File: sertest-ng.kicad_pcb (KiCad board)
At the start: 4 copper layers, 50 x 160 mm, 145 parts, among them J101 SWD, J102 USB, J201 Debug, J202 RS-232, J203 RS-485/422, J301 USB, J401 CAN, J402 CAN, SW101 Reset, SW401 Term, U101 M24C64-RMN, U102 AMS1117-3.3, U103 STM32G431RBTx, U104 ATECC608B-MAVDA-S, U105 USBLC6-2SC6, U201 ADM213, U202 SP330, U301 XC6206P332MR, U302 CH340N, U303 USBLC6-2SC6, U401 TJA1042T, Y101 8MHz, Y102 32k

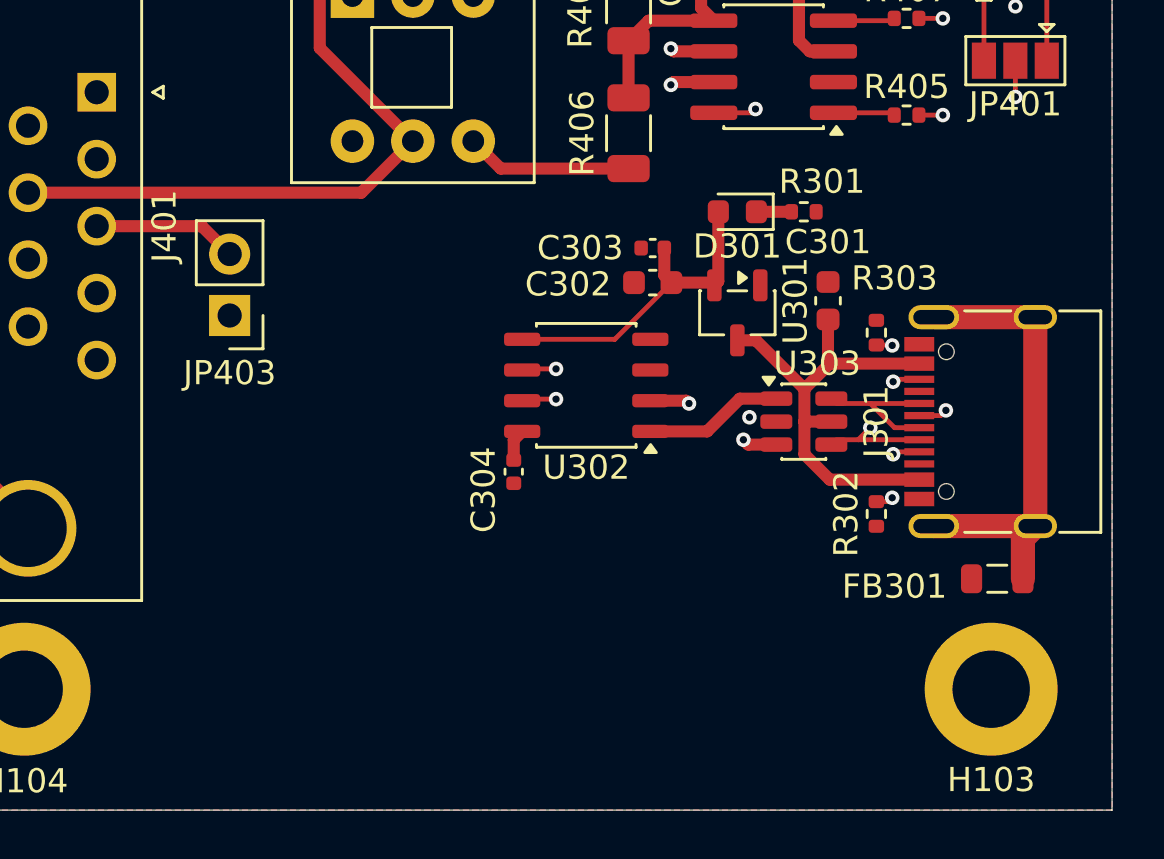
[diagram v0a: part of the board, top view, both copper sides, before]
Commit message: Revisit 3D models
Signed-off-by: Benedikt Spranger <b.spranger@linutronix.de>
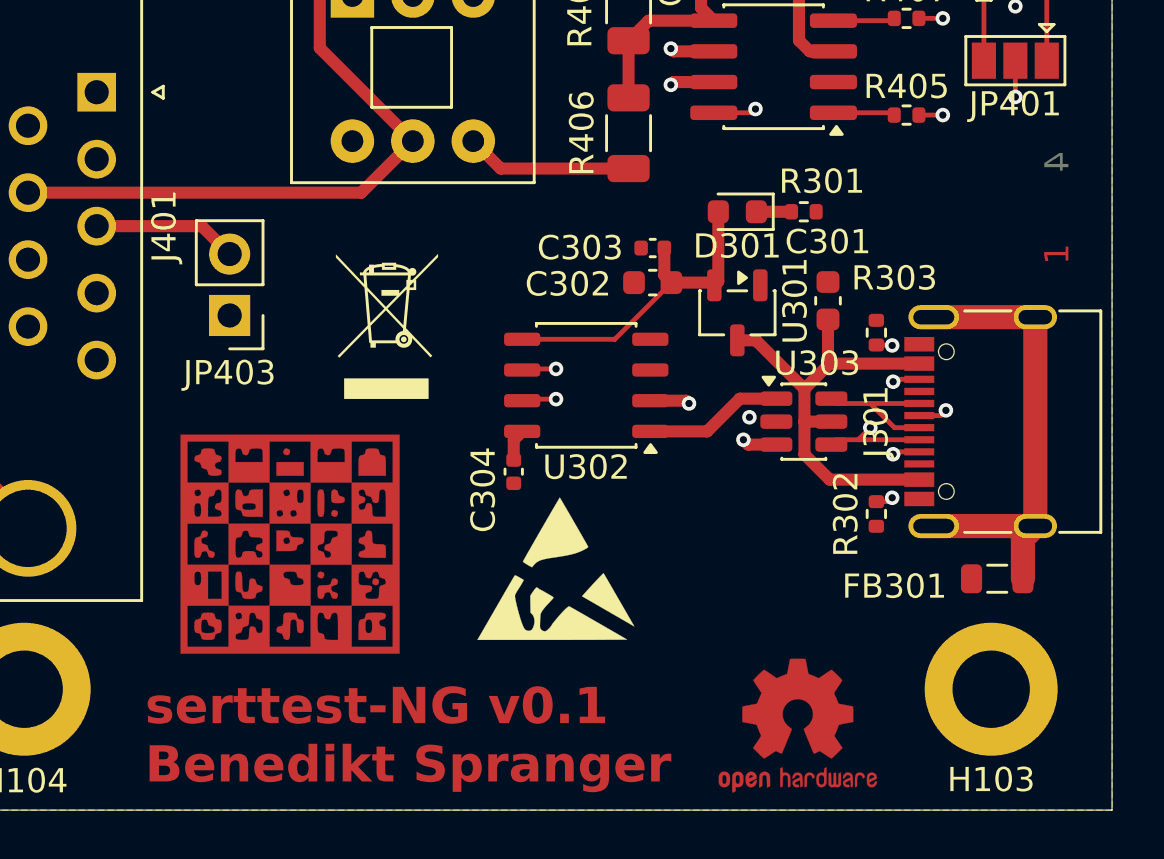
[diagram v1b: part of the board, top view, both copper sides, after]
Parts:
- added G***: LOGO, eurovibes:LOGO, F.Cu at (106.0, 169.0)
- added REF**: OSHW-Logo2_7.3x6mm_Copper, Symbol:OSHW-Logo2_7.3x6mm_Copper, F.Cu at (127.0, 176.5)
- added REF**: LayerMarker_4_6.35x2.54mm_TextH1mm_P1.27mm_BottomMirrored, Symbol:LayerMarker_4_6.35x2.54mm_TextH1mm_P1.27mm_BottomMirrored, F.Cu at (139.0, 157.0)
- added REF**: WEEE-Logo_4.2x6mm_SilkScreen, Symbol:WEEE-Logo_4.2x6mm_SilkScreen, F.Cu at (110.0, 160.0)
- added REF**: ESD-Logo_6.6x6mm_SilkScreen, Symbol:ESD-Logo_6.6x6mm_SilkScreen, F.Cu at (117.0, 170.0)
- D201, D202, D203, D204, D205, D206, D207, D208, D209, D210, D211, D212, D213, D214, D401, D402: footprint LED_SMD:LED_Kingbright_AAA3528ESGCT -> fixes:LED_Kingbright_AAA3528ESGCT
- J203: footprint TerminalBlock_WAGO:TerminalBlock_WAGO_236-404_1x04_P5.00mm_45Degree -> fixes:TerminalBlock_WAGO_236-404_1x04_P5.00mm_45Degree
- J402: footprint TerminalBlock_WAGO:TerminalBlock_WAGO_236-402_1x02_P5.00mm_45Degree -> fixes:TerminalBlock_WAGO_236-402_1x02_P5.00mm_45Degree
- SW401: footprint Button_Switch_THT:SW_Push_2P2T_Toggle_CK_PVA2xxH1xxxxxxV2 -> fixes:SW_Push_2P2T_Toggle_CK_PVA2xxH1xxxxxxV2
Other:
- board text added: "serttest-NG v0.1 Benedikt Spranger"

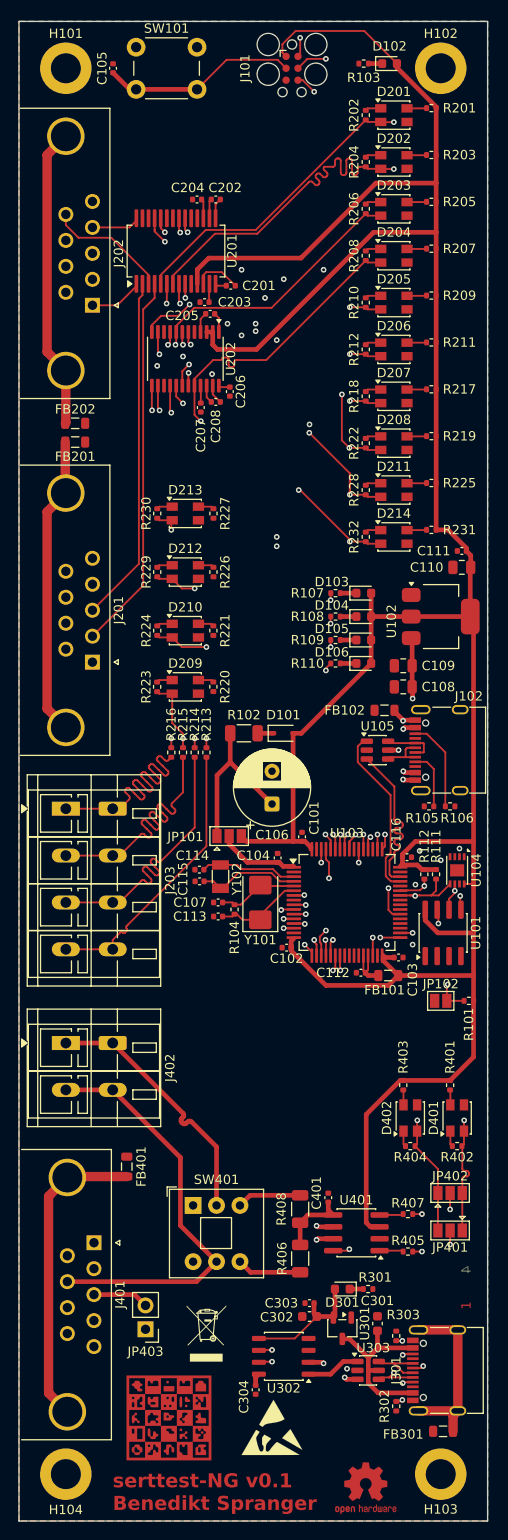
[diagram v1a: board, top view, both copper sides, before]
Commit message: Fix Dual LED footprint issue
Signed-off-by: Benedikt Spranger <b.spranger@linutronix.de>
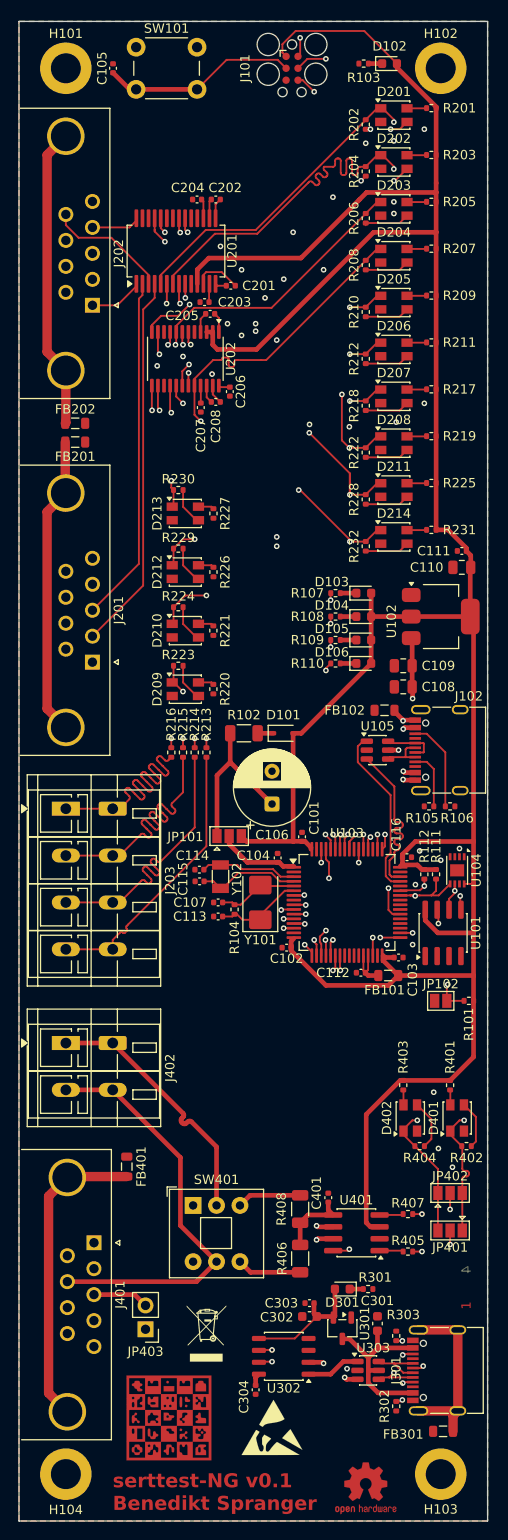
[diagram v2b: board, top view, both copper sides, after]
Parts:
- moved R224 3.36 mm to (107.0, 82.5), turned to 0 degrees
- moved R229 3.36 mm to (107.0, 76.2), turned to 0 degrees
- moved R230 3.36 mm to (107.0, 70.0), turned to 0 degrees
- moved R223 3.19 mm to (107.0, 88.8), turned to 0 degrees
- moved R202 1.00 mm to (127.0, 31.0), turned to -90 degrees
- moved R204 1.00 mm to (127.0, 36.0), turned to -90 degrees
- moved R206 1.00 mm to (127.0, 41.0), turned to -90 degrees
- moved R208 1.00 mm to (127.0, 46.0), turned to -90 degrees
- moved R210 1.00 mm to (127.0, 51.0), turned to -90 degrees
- moved R212 1.00 mm to (127.0, 56.0), turned to -90 degrees
- moved R218 1.00 mm to (127.0, 61.0), turned to -90 degrees
- moved R222 1.00 mm to (127.0, 66.0), turned to -90 degrees
- moved R228 1.00 mm to (127.0, 71.0), turned to -90 degrees
- moved R232 1.00 mm to (127.0, 76.0), turned to -90 degrees
- moved R402 1.00 mm to (137.8, 140.0), turned to 0 degrees
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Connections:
- D201 pad 1: Net-(D201-A1) -> /USART3_RX
- D201 pad 3: GND -> Net-(D201-A1)
- D201 pad 4: /USART3_RX -> GND
- D202 pad 1: Net-(D202-A1) -> /USART3_TX
- D202 pad 3: GND -> Net-(D202-A1)
- D202 pad 4: /USART3_TX -> GND
- D203 pad 1: Net-(D203-A1) -> /USART2_RX
- D203 pad 3: GND -> Net-(D203-A1)
- D203 pad 4: /USART2_RX -> GND
- D204 pad 1: Net-(D204-A1) -> /USART2_TX
- D204 pad 3: GND -> Net-(D204-A1)
- D204 pad 4: /USART2_TX -> GND
- D205 pad 1: Net-(D205-A1) -> /USART2_CTS
- D205 pad 3: GND -> Net-(D205-A1)
- D205 pad 4: /USART2_CTS -> GND
- D206 pad 1: Net-(D206-A1) -> /USART2_RTS
- D206 pad 3: GND -> Net-(D206-A1)
- D206 pad 4: /USART2_RTS -> GND
- D207 pad 1: Net-(D207-A1) -> /USART2_DCD
- D207 pad 3: GND -> Net-(D207-A1)
- D207 pad 4: /USART2_DCD -> GND
- D208 pad 1: Net-(D208-A1) -> /USART2_DSR
- D208 pad 3: GND -> Net-(D208-A1)
- D208 pad 4: /USART2_DSR -> GND
- D209 pad 1: Net-(D209-A1) -> /Serial/TXD
- D209 pad 3: GND -> Net-(D209-A1)
- D209 pad 4: /Serial/TXD -> GND
- D210 pad 1: Net-(D210-A1) -> /Serial/RXD
- D210 pad 3: GND -> Net-(D210-A1)
- D210 pad 4: /Serial/RXD -> GND
- D211 pad 1: Net-(D211-A1) -> /USART2_DTR
- D211 pad 3: GND -> Net-(D211-A1)
- D211 pad 4: /USART2_DTR -> GND
- D212 pad 1: Net-(D212-A1) -> /Serial/CTS
- D212 pad 3: GND -> Net-(D212-A1)
- D212 pad 4: /Serial/CTS -> GND
- D213 pad 1: Net-(D213-A1) -> /Serial/RTS
- D213 pad 3: GND -> Net-(D213-A1)
- D213 pad 4: /Serial/RTS -> GND
- D214 pad 1: Net-(D214-A1) -> /USART2_RI
- D214 pad 3: GND -> Net-(D214-A1)
- D214 pad 4: /USART2_RI -> GND
- D401 pad 1: Net-(D401-A1) -> /FDCAN1_TX
- D401 pad 3: GND -> Net-(D401-A1)
- D401 pad 4: /FDCAN1_TX -> GND
- D402 pad 1: Net-(D402-A1) -> /FDCAN1_RX
- D402 pad 3: GND -> Net-(D402-A1)
- D402 pad 4: /FDCAN1_RX -> GND
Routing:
- net Net-(D202-A1): track 1.69 -> 6.13 mm, vias 0 -> 2
- net Net-(D402-A1): track 1.69 -> 5.34 mm
- net /Serial/TXD: track 69.2 -> 65.7 mm, vias 2 -> 3
- net Net-(D203-A1): track 1.69 -> 5.18 mm
- net Net-(D401-A1): track 1.69 -> 5.13 mm
- net Net-(D214-A1): track 1.69 -> 4.73 mm
- net Net-(D211-A1): track 1.69 -> 4.73 mm
- net Net-(D208-A1): track 1.69 -> 4.73 mm
- net Net-(D201-A1): track 1.69 -> 4.73 mm, vias 0 -> 2
- net Net-(D207-A1): track 1.69 -> 4.73 mm
- net Net-(D206-A1): track 1.69 -> 4.73 mm
- net Net-(D205-A1): track 1.69 -> 4.73 mm
- net Net-(D204-A1): track 1.69 -> 4.73 mm
- net Net-(D213-A1): track 1.69 -> 4.02 mm
- net Net-(D212-A1): track 1.69 -> 4.02 mm
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
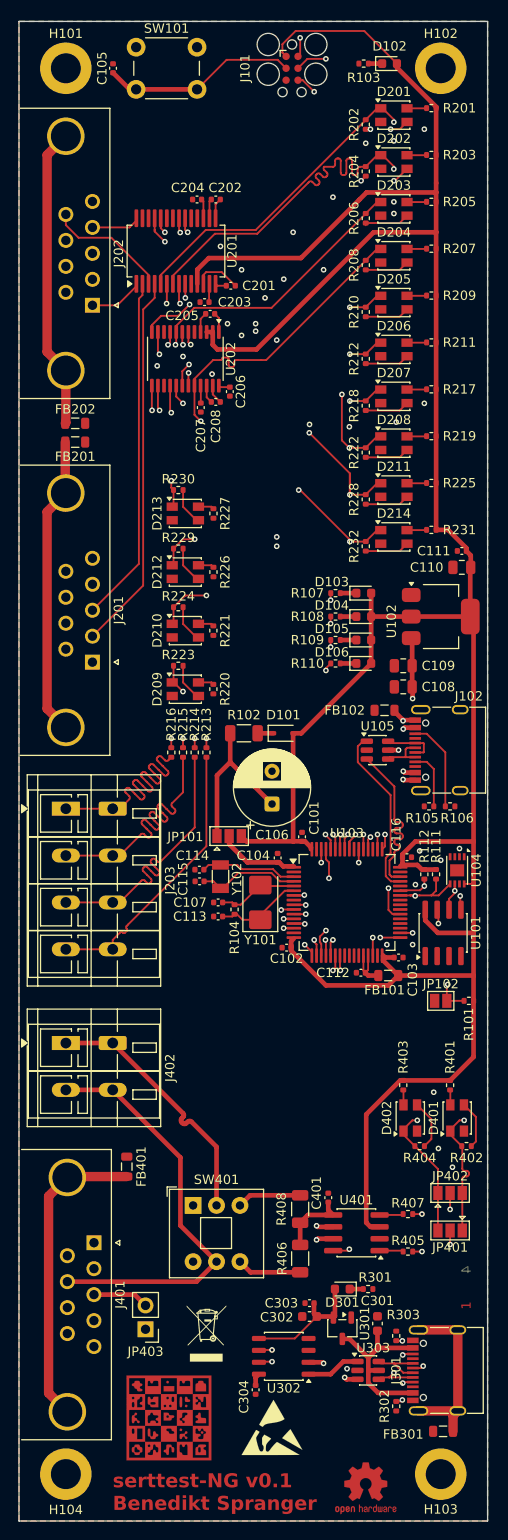
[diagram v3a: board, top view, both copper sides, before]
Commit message: Swap USART1 RX/TX
Signed-off-by: Benedikt Spranger <b.spranger@linutronix.de>
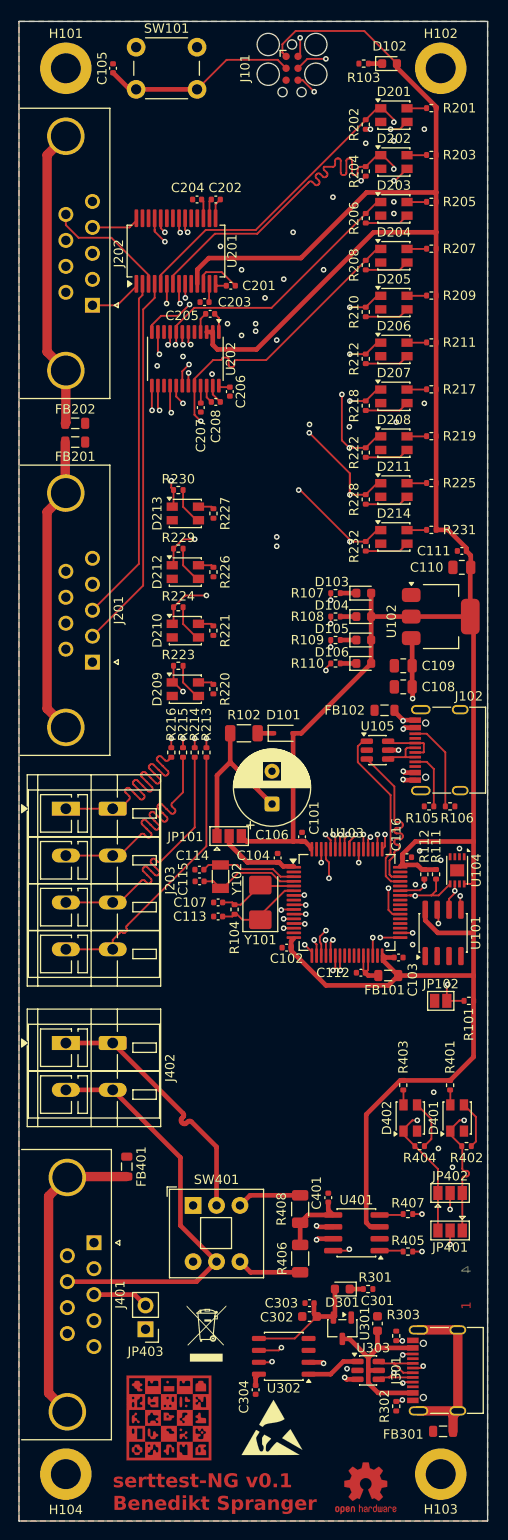
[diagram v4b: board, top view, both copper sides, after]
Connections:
- U302 pad 6: /USART1_TX -> /USART1_RX
- U302 pad 7: /USART1_RX -> /USART1_TX
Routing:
- net /Serial/RI: track 14.1 -> 13.1 mm
- net /USART2_RX: track 100.6 -> 99.8 mm
- net /Serial/Y: track 30.0 -> 29.2 mm
- net /~{RST}: track 115.5 -> 114.8 mm
- net /FDCAN1_TX: track 49.4 -> 48.8 mm
- net /FDCAN1_RX: track 49.4 -> 48.8 mm
- net /USART3_TX: track 127.7 -> 127.2 mm
- net /USART3_RX: track 127.9 -> 127.3 mm

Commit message: Rework serial from DTE to DCE
Signed-off-by: Benedikt Spranger <b.spranger@linutronix.de>
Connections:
- J201 pad 2: Net-(U201-R2IN) -> Net-(U201-T1OUT)
- J201 pad 3: Net-(U201-T1OUT) -> Net-(U201-R2IN)
- J202 pad 2: /Serial/TXD -> /Serial/RXD
- J202 pad 3: /Serial/RXD -> /Serial/TXD
- J202 pad 7: /Serial/CTS -> /Serial/RTS
- J202 pad 8: /Serial/RTS -> /Serial/CTS
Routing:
- net /Serial/TXD: track 65.3 -> 69.4 mm
- net Net-(U201-T1OUT): track 36.8 -> 39.6 mm
- net /Serial/RXD: track 73.1 -> 71.2 mm, vias 3 -> 4
- net /Serial/RTS: track 71.7 -> 69.9 mm
- net /Serial/CTS: track 71.7 -> 69.9 mm
- net Net-(U201-R2IN): track 40.1 -> 39.4 mm, vias 0 -> 1

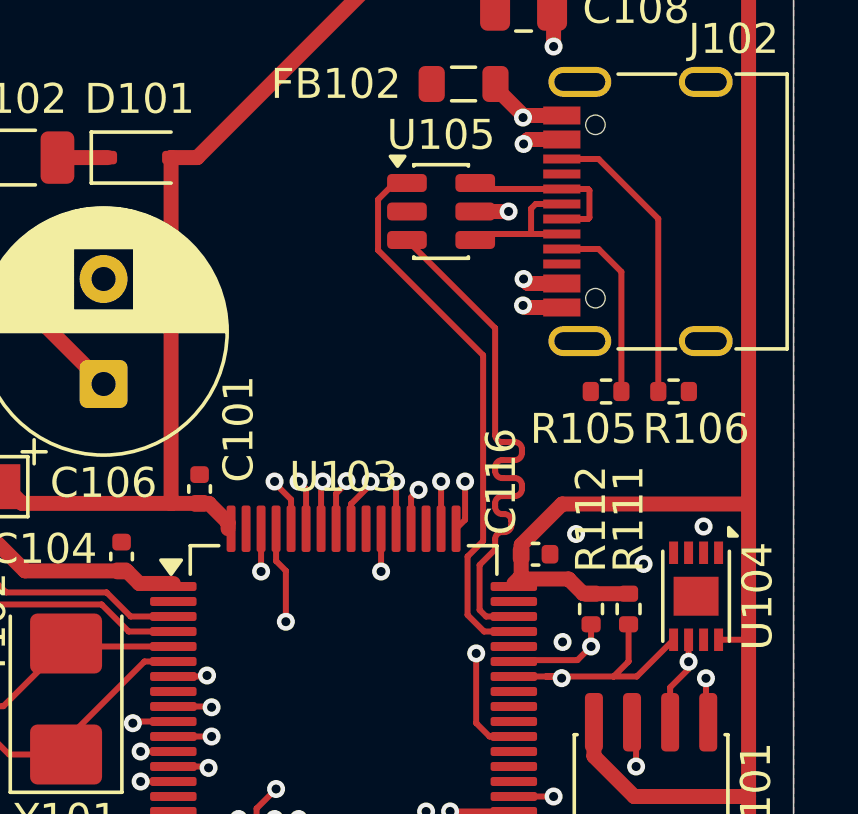
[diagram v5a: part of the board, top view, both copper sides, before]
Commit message: Fix USB signal swap
Signed-off-by: Benedikt Spranger <bene@eurovibes.org>
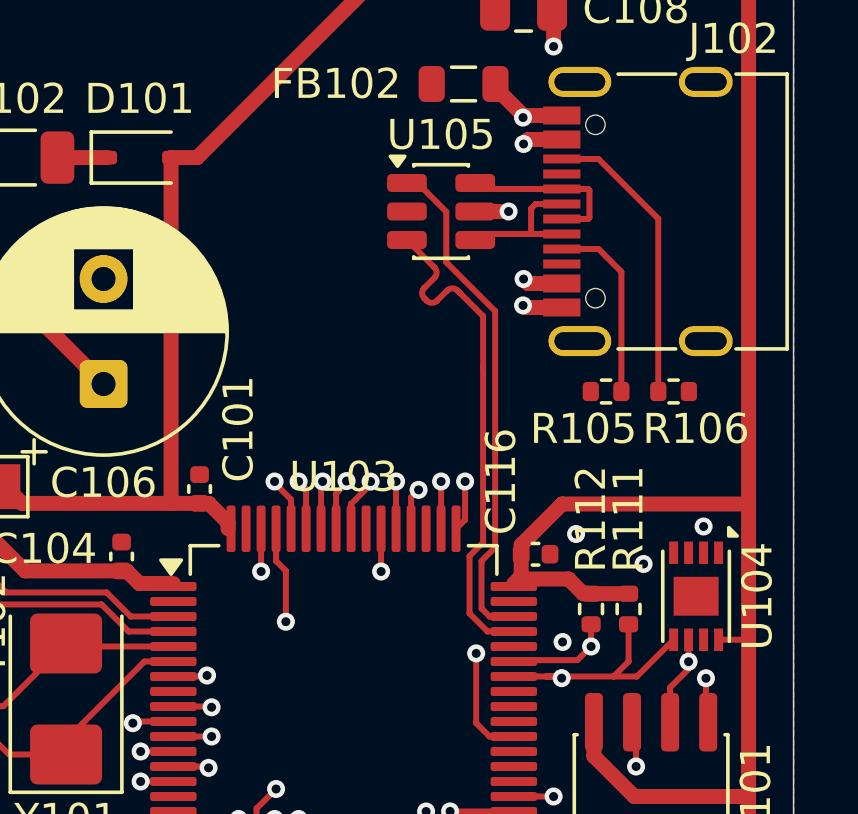
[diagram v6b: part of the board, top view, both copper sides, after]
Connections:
- U105 pad 1: /USB_DM -> /USB_DP
- U105 pad 3: /USB_DP -> /USB_DM
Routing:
- net /USB_DP: track 18.3 -> 17.0 mm
- net /USB_DM: track 18.1 -> 16.9 mm

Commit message: Add USB termination resistors
Signed-off-by: Benedikt Spranger <b.spranger@linutronix.de>
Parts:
- added R108: 33, Resistor_SMD:R_0402_1005Metric, F.Cu at (130.2, 103.2)
- added R109: 33, Resistor_SMD:R_0402_1005Metric, F.Cu at (129.0, 103.2)
- renumbered C107 to C101, C113 to C102, C114 to C103, C115 to C104, C106 to C105, C105 to C106, C108 to C107, C116 to C108, C101 to C110, C102 to C111, C110 to C112, C103 to C113, C111 to C114, C104 to C115, C112 to C116, D103 to D102, D104 to D103, D105 to D104, D106 to D105, D102 to D106, FB102 to FB101, FB101 to FB102, J102 to J101, J101 to J102, JP102 to JP101, JP101 to JP102, JP403 to JP401, JP401 to JP402, JP402 to JP403, R111 to R102, R112 to R103, R105 to R104, R106 to R105, R104 to R106, R102 to R107, R107 to R110, R108 to R111, R109 to R112, R110 to R113, R103 to R114, R302 to R301, R303 to R302, R301 to R303, R406 to R405, R408 to R406, R405 to R407, R407 to R408, U105 to U102, U102 to U105, U303 to U301, U301 to U302, U302 to U303
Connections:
- U102 pad 1: /USB_DP -> Net-(R108-Pad1)
- U102 pad 3: /USB_DM -> Net-(R109-Pad2)
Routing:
- net Net-(R108-Pad1): track 0.00 -> 7.63 mm
- net Net-(R109-Pad2): track 0.00 -> 7.55 mm
- net /USB_DP: track 17.0 -> 9.53 mm
- net /USB_DM: track 16.9 -> 9.57 mm
